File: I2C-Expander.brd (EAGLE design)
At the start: 106 x 100 mm, 79 parts, among them IC1 MCP23017SO, IC2 PCA9555D, Q0 P-FET, Q1 P-FET, Q10 P-FET, Q11 P-FET, Q12 P-FET, Q13 P-FET, Q14 P-FET, Q15 P-FET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

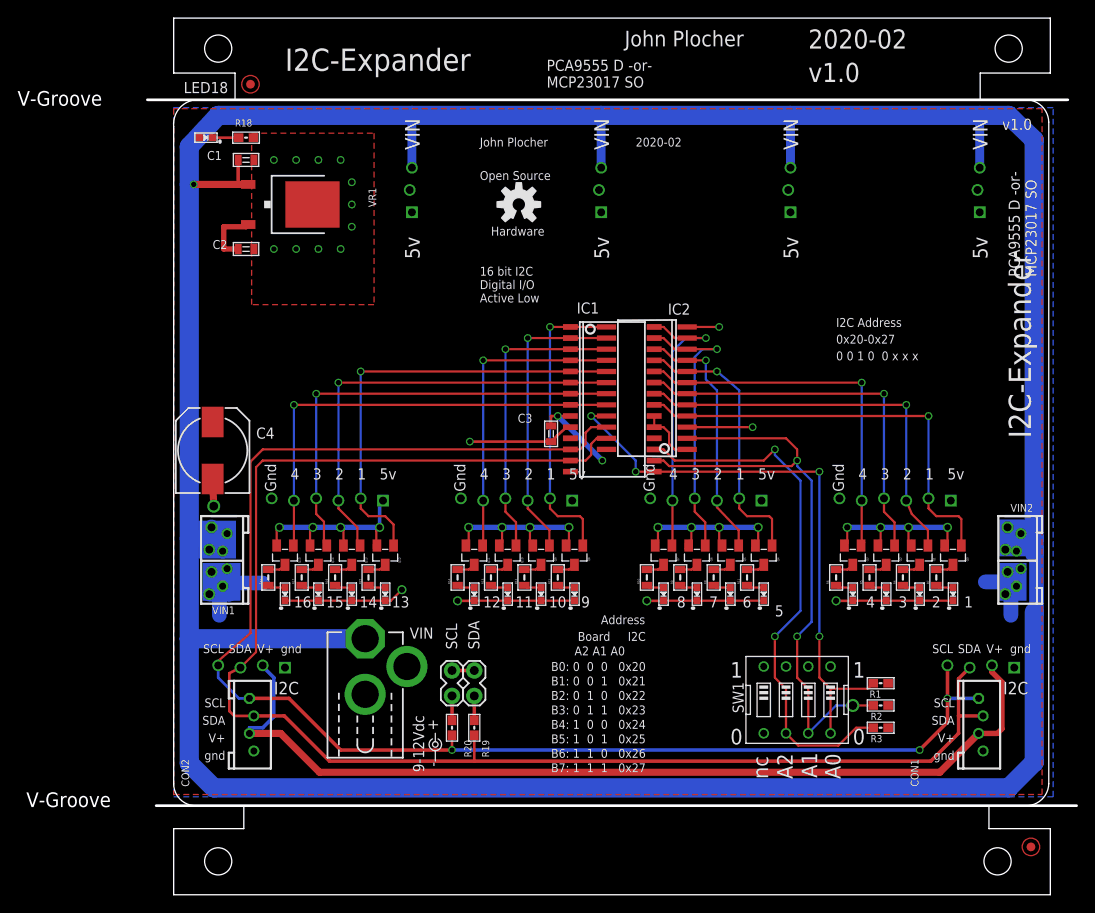
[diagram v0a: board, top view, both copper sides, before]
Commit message: added LED on input changed interrupt pins
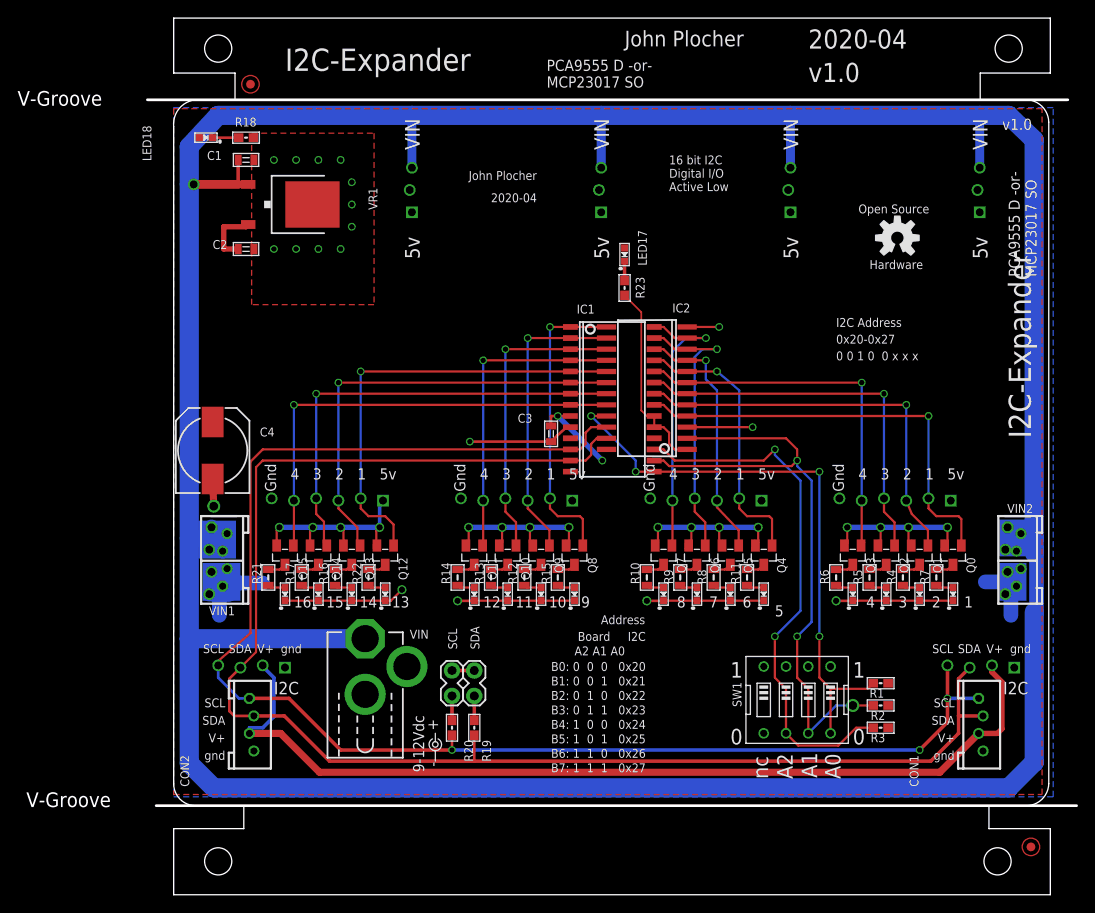
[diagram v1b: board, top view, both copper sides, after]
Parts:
- added LED17: GREEN, SPCoast:0603-LED
- added R23: 2K2, SPCoast:0603-RES
- moved OSHW1 43.3 mm to (82.5, 74.9)
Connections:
- new net N$19: LED17.C, R23.1
- net !INT: now also R23.2
- net VCC: now also LED17.A
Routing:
- net !INT: track 6.82 -> 22.5 mm
- net N$19: track 0.00 -> 2.21 mm
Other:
- board text added: "2020-04"
- board text removed: "2020-02"

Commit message: fixed SPCoast lbr part orientation
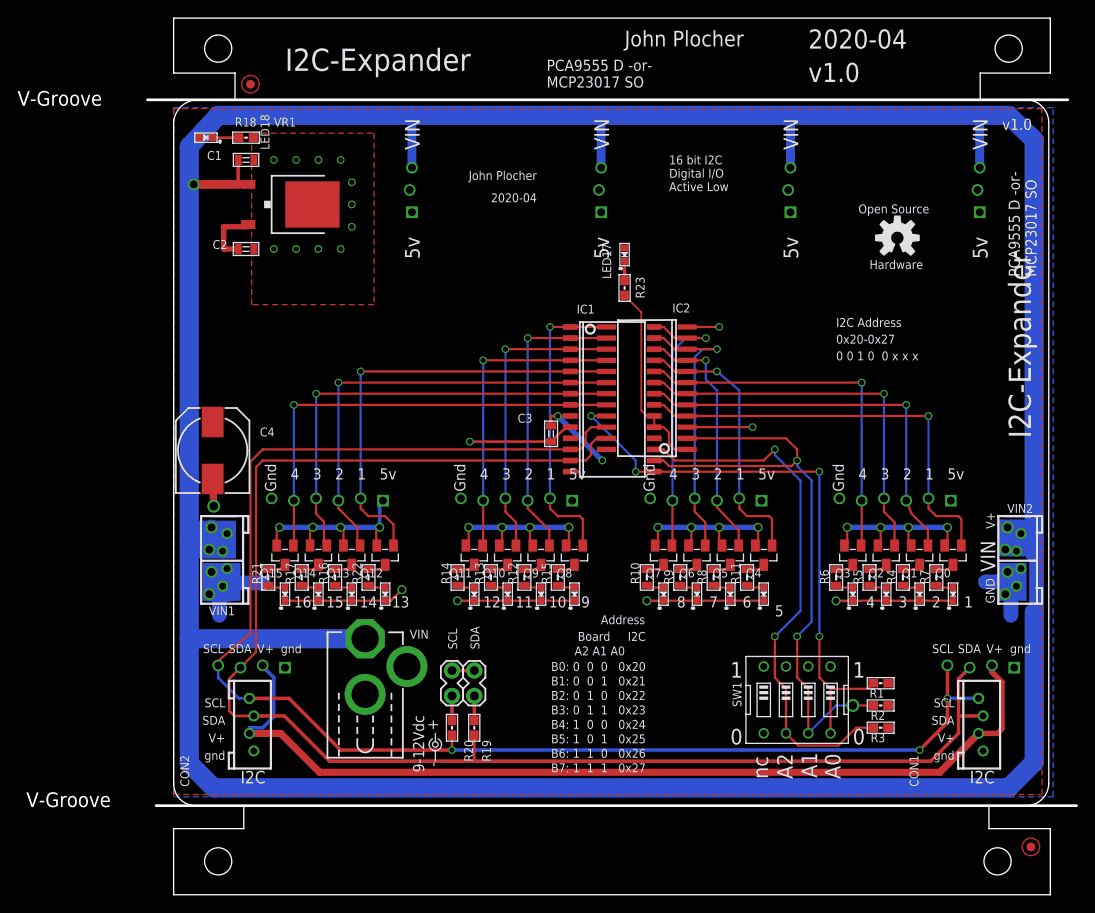
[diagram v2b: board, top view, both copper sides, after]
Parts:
- R18, R23: value 2K2 -> 4k7
- turned LED1 to 90 degrees
- turned LED10 to 90 degrees
- turned LED11 to 90 degrees
- turned LED12 to 90 degrees
- turned LED13 to 90 degrees
- turned LED14 to 90 degrees
- turned LED15 to 90 degrees
- turned LED16 to 90 degrees
- turned LED17 to 90 degrees
- turned LED18 to 180 degrees
- turned LED2 to 90 degrees
- turned LED3 to 90 degrees
- turned LED4 to 90 degrees
- turned LED5 to 90 degrees
- turned LED6 to 90 degrees
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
